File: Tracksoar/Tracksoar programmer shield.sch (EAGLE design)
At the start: 10 parts, among them U1 FT232RL-BASICSSOP

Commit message: removed old shields
removed square shields and added values to shield passives
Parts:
- C1: value (none) -> 100pf
- C2: value (none) -> 10uf
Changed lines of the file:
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@@
 <part name="LED2" library="adafruit" deviceset="LED" device="CHIP-LED0805"/>
 <part name="JP2" library="SparkFun-Connectors" deviceset="AVR_SPI_PRG_6" device="PTH"/>
-<part name="C1" library="SparkFun-Capacitors" deviceset="CAP" device="0805"/>
-<part name="C2" library="SparkFun-Capacitors" deviceset="CAP" device="0805"/>
+<part name="C1" library="SparkFun-Capacitors" deviceset="CAP" device="0805" value="100pf"/>
+<part name="C2" library="SparkFun-Capacitors" deviceset="CAP" device="0805" value="10uf"/>
 </parts>
 <sheets>

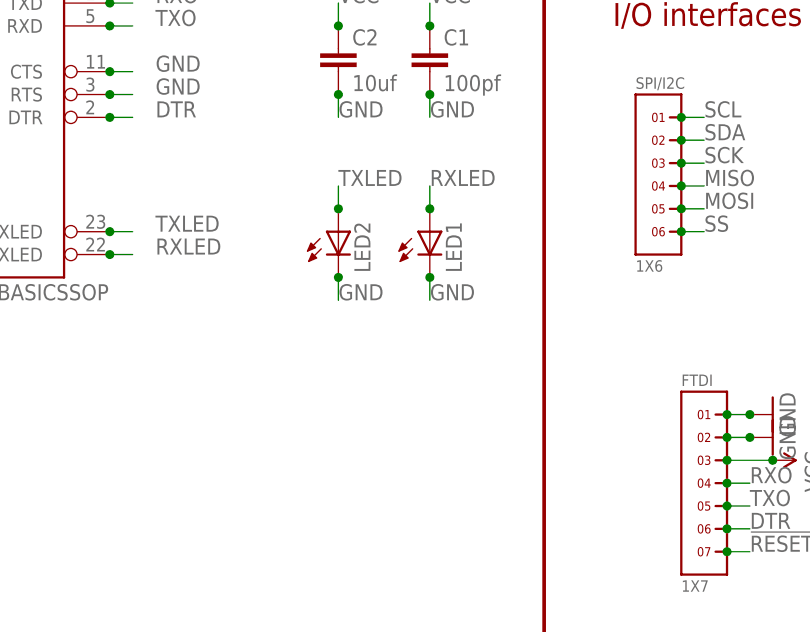
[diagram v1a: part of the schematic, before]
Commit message: updates
added twometertx-micrf300, changed layout of twometertx, changed led
layout on programmer shield to correct an error, added tracksoar v1.1
to swap power and ground pins on power input header
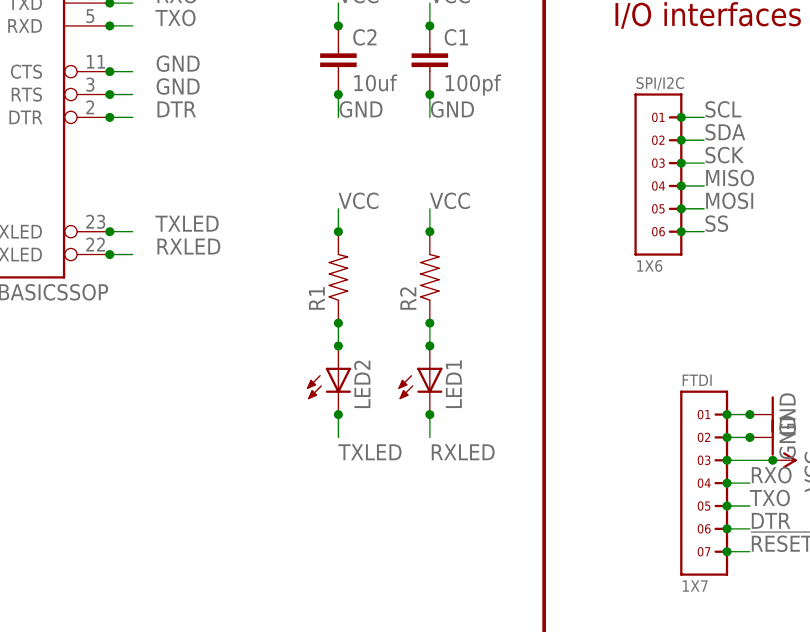
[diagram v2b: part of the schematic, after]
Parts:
- added R1, R2: (no value), SparkFun-Passives:RESISTOR0805-RES
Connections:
- new net N$1: LED2.A, R1.1
- new net N$2: LED1.A, R2.1
- net GND: no longer LED1.C, LED2.C
- net RXLED: now also LED1.C; no longer LED1.A
- net TXLED: now also LED2.C; no longer LED2.A
- net VCC: now also R1.2, R2.2
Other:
- moved on the sheet: LED1, LED2
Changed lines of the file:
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@@
 <?xml version="1.0" encoding="utf-8"?>
 <!DOCTYPE eagle SYSTEM "eagle.dtd">
-<eagle version="7.3.0">
+<eagle version="7.5.0">
 <drawing>
 <settings>
@@
 <layers>
 <layer number="1" name="Top" color="4" fill="1" visible="no" active="no"/>
+<layer number="2" name="Route2" color="1" fill="3" visible="no" active="no"/>
+<layer number="3" name="Route3" color="4" fill="3" visible="no" active="no"/>
+<layer number="14" name="Route14" color="1" fill="6" visible="no" active="no"/>
+<layer number="15" name="Route15" color="4" fill="6" visible="no" active="no"/>
 <layer number="16" name="Bottom" color="1" fill="1" visible="no" active="no"/>
 <layer number="17" name="Pads" color="2" fill="1" visible="no" active="no"/>
@@
 <part name="C1" library="SparkFun-Capacitors" deviceset="CAP" device="0805" value="100pf"/>
 <part name="C2" library="SparkFun-Capacitors" deviceset="CAP" device="0805" value="10uf"/>
+<part name="R1" library="SparkFun-Passives" deviceset="RESISTOR" device="0805-RES"/>
+<part name="R2" library="SparkFun-Passives" deviceset="RESISTOR" device="0805-RES"/>
 </parts>
 <sheets>
@@
 <instance part="JP1" gate="G$1" x="233.68" y="93.98" rot="R180"/>
 <instance part="U1" gate="G$1" x="119.38" y="93.98"/>
-<instance part="LED1" gate="G$1" x="170.18" y="81.28"/>
-<instance part="LED2" gate="G$1" x="160.02" y="81.28"/>
+<instance part="LED1" gate="G$1" x="170.18" y="66.04"/>
+<instance part="LED2" gate="G$1" x="160.02" y="66.04"/>
 <instance part="JP2" gate="G$1" x="228.6" y="68.58"/>
 <instance part="C1" gate="G$1" x="170.18" y="99.06"/>
 <instance part="C2" gate="G$1" x="160.02" y="99.06"/>
+<instance part="R1" gate="G$1" x="160.02" y="76.2" rot="R90"/>
+<instance part="R2" gate="G$1" x="170.18" y="76.2" rot="R90"/>
 </instances>
 <busses>
@@
 </segment>
 <segment>
-<pinref part="LED2" gate="G$1" pin="C"/>
-<wire x1="160.02" y1="76.2" x2="160.02" y2="73.66" width="0.1524" layer="91"/>
-<junction x="160.02" y="76.2"/>
-<label x="160.02" y="73.66" size="1.778" layer="95"/>
-</segment>
-<segment>
-<pinref part="LED1" gate="G$1" pin="C"/>
-<wire x1="170.18" y1="76.2" x2="170.18" y2="73.66" width="0.1524" layer="91"/>
-<junction x="170.18" y="76.2"/>
-<label x="170.18" y="73.66" size="1.778" layer="95"/>
-</segment>
-<segment>
 <pinref part="JP1" gate="G$1" pin="GND"/>
 <wire x1="236.22" y1="93.98" x2="238.76" y2="93.98" width="0.1524" layer="91"/>
@@
 <junction x="238.76" y="71.12"/>
 </segment>
+<segment>
+<pinref part="R1" gate="G$1" pin="2"/>
+<wire x1="160.02" y1="81.28" x2="160.02" y2="83.82" width="0.1524" layer="91"/>
+<junction x="160.02" y="81.28"/>
+<label x="160.02" y="83.82" size="1.778" layer="95"/>
+</segment>
+<segment>
+<pinref part="R2" gate="G$1" pin="2"/>
+<wire x1="170.18" y1="81.28" x2="170.18" y2="83.82" width="0.1524" layer="91"/>
+<junction x="170.18" y="81.28"/>
+<label x="170.18" y="83.82" size="1.778" layer="95"/>
+</segment>
 </net>
 <net name="DTR" class="0">
@@
 </segment>
 <segment>
-<pinref part="LED2" gate="G$1" pin="A"/>
-<wire x1="160.02" y1="83.82" x2="160.02" y2="86.36" width="0.1524" layer="91"/>
-<junction x="160.02" y="83.82"/>
-<label x="160.02" y="86.36" size="1.778" layer="95"/>
+<pinref part="LED2" gate="G$1" pin="C"/>
+<wire x1="160.02" y1="60.96" x2="160.02" y2="58.42" width="0.1524" layer="91"/>
+<junction x="160.02" y="60.96"/>
+<label x="160.02" y="55.88" size="1.778" layer="95"/>
 </segment>
 </net>
@@
 </segment>
 <segment>
+<pinref part="LED1" gate="G$1" pin="C"/>
+<wire x1="170.18" y1="60.96" x2="170.18" y2="58.42" width="0.1524" layer="91"/>
+<junction x="170.18" y="60.96"/>
+<label x="170.18" y="55.88" size="1.778" layer="95"/>
+</segment>
+</net>
+<net name="N$1" class="0">
+<segment>
+<pinref part="LED2" gate="G$1" pin="A"/>
+<pinref part="R1" gate="G$1" pin="1"/>
+<wire x1="160.02" y1="71.12" x2="160.02" y2="68.58" width="0.1524" layer="91"/>
+<junction x="160.02" y="71.12"/>
+<junction x="160.02" y="68.58"/>
+</segment>
+</net>
+<net name="N$2" class="0">
+<segment>
 <pinref part="LED1" gate="G$1" pin="A"/>
-<wire x1="170.18" y1="83.82" x2="170.18" y2="86.36" width="0.1524" layer="91"/>
-<junction x="170.18" y="83.82"/>
-<label x="170.18" y="86.36" size="1.778" layer="95"/>
-</segment>
-</net>
+<pinref part="R2" gate="G$1" pin="1"/>
+<wire x1="170.18" y1="71.12" x2="170.18" y2="68.58" width="0.1524" layer="91"/>
+<junction x="170.18" y="71.12"/>
+<junction x="170.18" y="68.58"/>
+</segment>
+</net>
